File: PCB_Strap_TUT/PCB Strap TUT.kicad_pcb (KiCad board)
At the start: 2 copper layers, 40.6 x 40.6 mm, 45 parts, among them J1 Debug, Q1 Q_PMOS_GDS, SW1 SW_SPST, U1 PIC16F1503-ISL

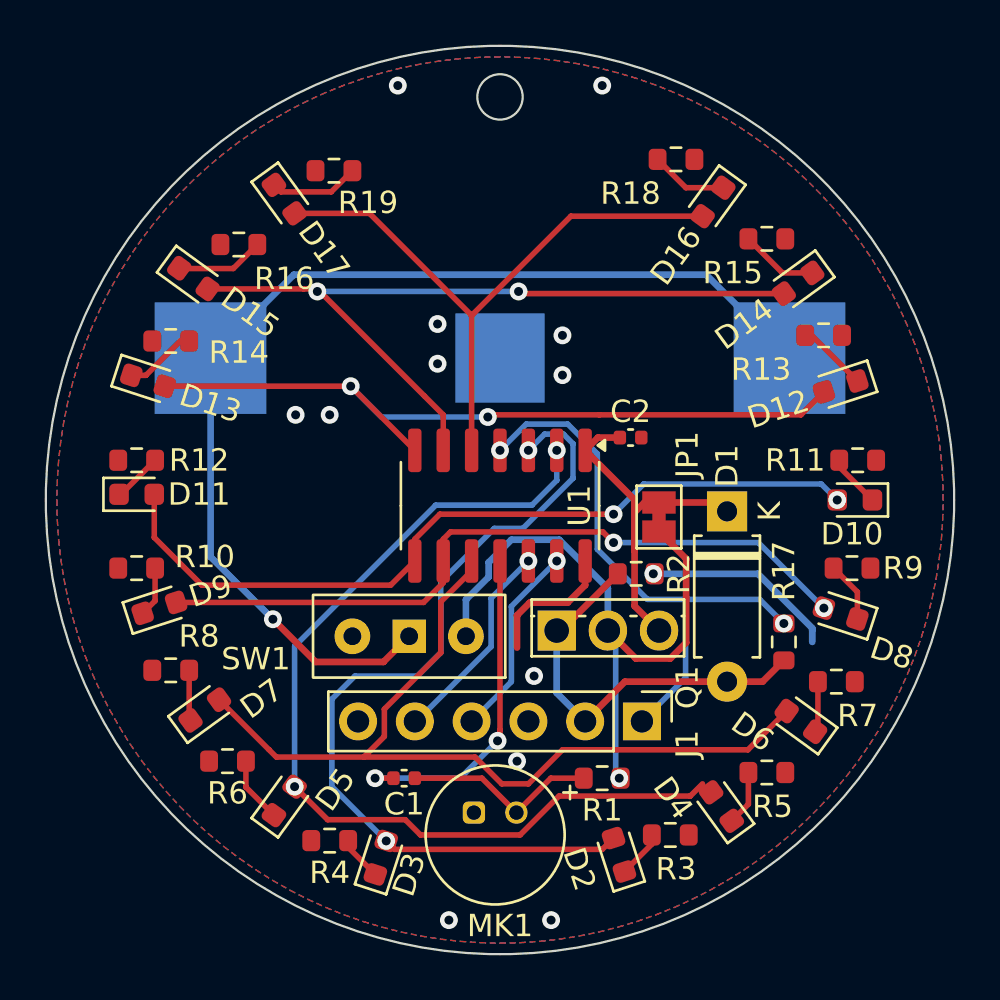
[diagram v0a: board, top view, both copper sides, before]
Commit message: test ADC and add Amp
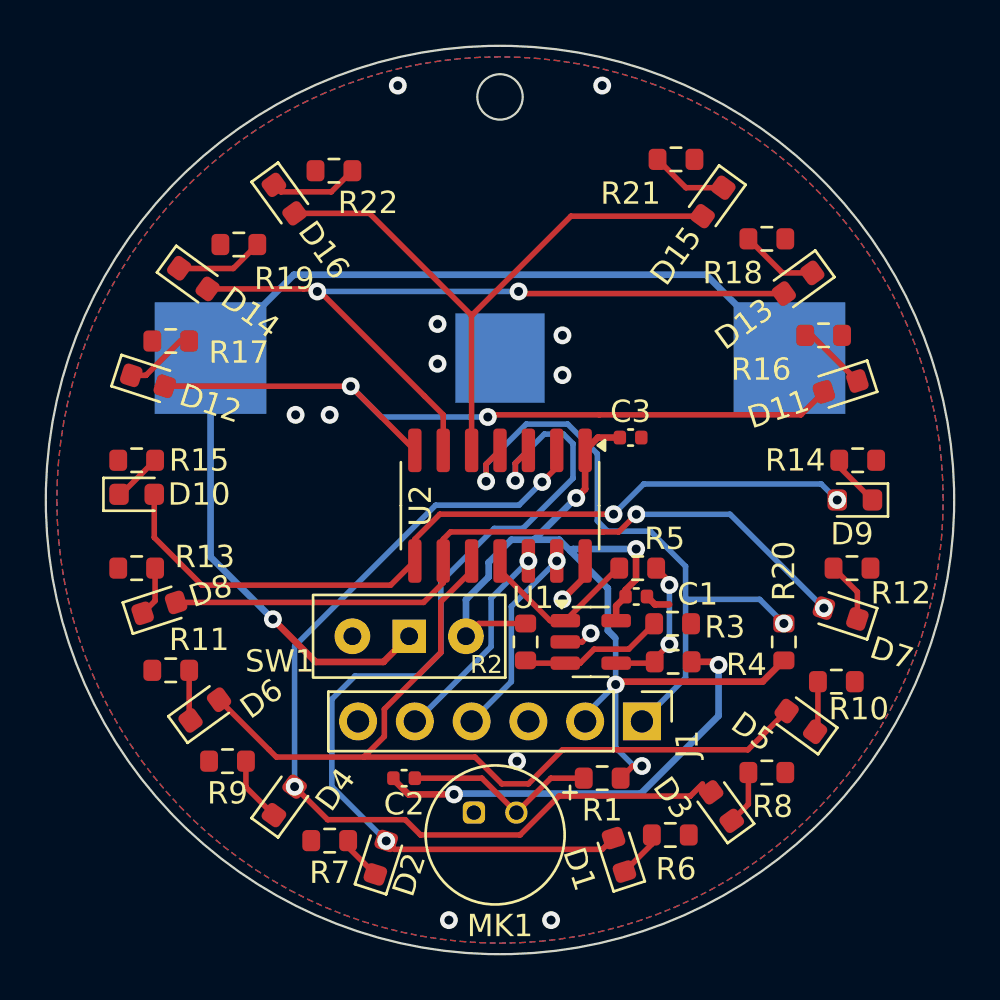
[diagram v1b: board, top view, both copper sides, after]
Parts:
- removed the D1 at (137.2, 95.8)
- removed JP1: POW_{SEL}, Jumper:SolderJumper-2_P1.3mm_Bridged_Pad1.0x1.5mm
- removed Q1: Q_PMOS_GDS, Package_TO_SOT_THT:TO-251-3_Vertical
- added C1: 100n, Capacitor_SMD:C_0402_1005Metric, F.Cu at (133.1, 99.6)
- added R3: 1k, Resistor_SMD:R_0603_1608Metric, F.Cu at (134.7, 102.5)
- added R4: 10k, Resistor_SMD:R_0603_1608Metric, F.Cu at (134.7, 100.8)
- added R5: 100k, Resistor_SMD:R_0603_1608Metric, F.Cu at (133.2, 98.3)
- added U1: MCP6401RT-xOT, Package_TO_SOT_SMD:SOT-23-5, F.Cu at (131.1, 101.6)
- C2: renamed from C1; value 4.7u -> 100n
- R2: value 100k -> 10k
- moved R2 5.82 mm to (128.1, 101.6), turned to 90 degrees
- renumbered C2 to C3, D2 to D1, D11 to D10, D12 to D11, D13 to D12, D14 to D13, D15 to D14, D16 to D15, D17 to D16, D3 to D2, D4 to D3, D5 to D4, D6 to D5, D7 to D6, D8 to D7, D9 to D8, D10 to D9, R7 to R10, R8 to R11, R9 to R12, R10 to R13, R11 to R14, R12 to R15, R13 to R16, R14 to R17, R15 to R18, R16 to R19, R17 to R20, R18 to R21, R19 to R22, R3 to R6, R4 to R7, R5 to R8, R6 to R9, U1 to U2
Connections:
- C2 pad 2: /RA2 -> Net-(C2-Pad2)
- C3 pad 1: VCC -> +3V0
- J1 pad 2: +5V -> +3V0
- R2 pad 1: +5V -> Net-(U1-+)
- R2 pad 2: GND -> +3V0
- R20 pad 2: +5V -> +3V0
- U2 pad 1: VCC -> +3V0
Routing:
- net Net-(C2-Pad2): track 0.00 -> 19.9 mm, vias 0 -> 2
- net +5V: track 18.4 -> 0.00 mm
- net +3V0: track 29.1 -> 46.9 mm, vias 1 -> 4
- net VCC: track 15.7 -> 0.00 mm
- net GND: track 14.9 -> 4.57 mm
- net /RA2: track 14.8 -> 7.67 mm, vias 2 -> 0
- net Net-(U1-+): track 0.00 -> 6.54 mm
- net Net-(U1--): track 0.00 -> 6.46 mm, vias 0 -> 2
- net /~{CLR}: track 25.7 -> 29.1 mm
- net /RA4: track 38.6 -> 41.8 mm
- net /RC1: track 32.8 -> 33.5 mm
